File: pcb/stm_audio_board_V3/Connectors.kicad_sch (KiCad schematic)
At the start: 11 parts, among them J1 Power conn, J2 STlink, J3 Audio_sig, J4 Conn_01x01_taptempo, J4 Conn_01x10_display, J6 Conn_01x03_pot_ext, J7 Conn_01x8_pots_internal

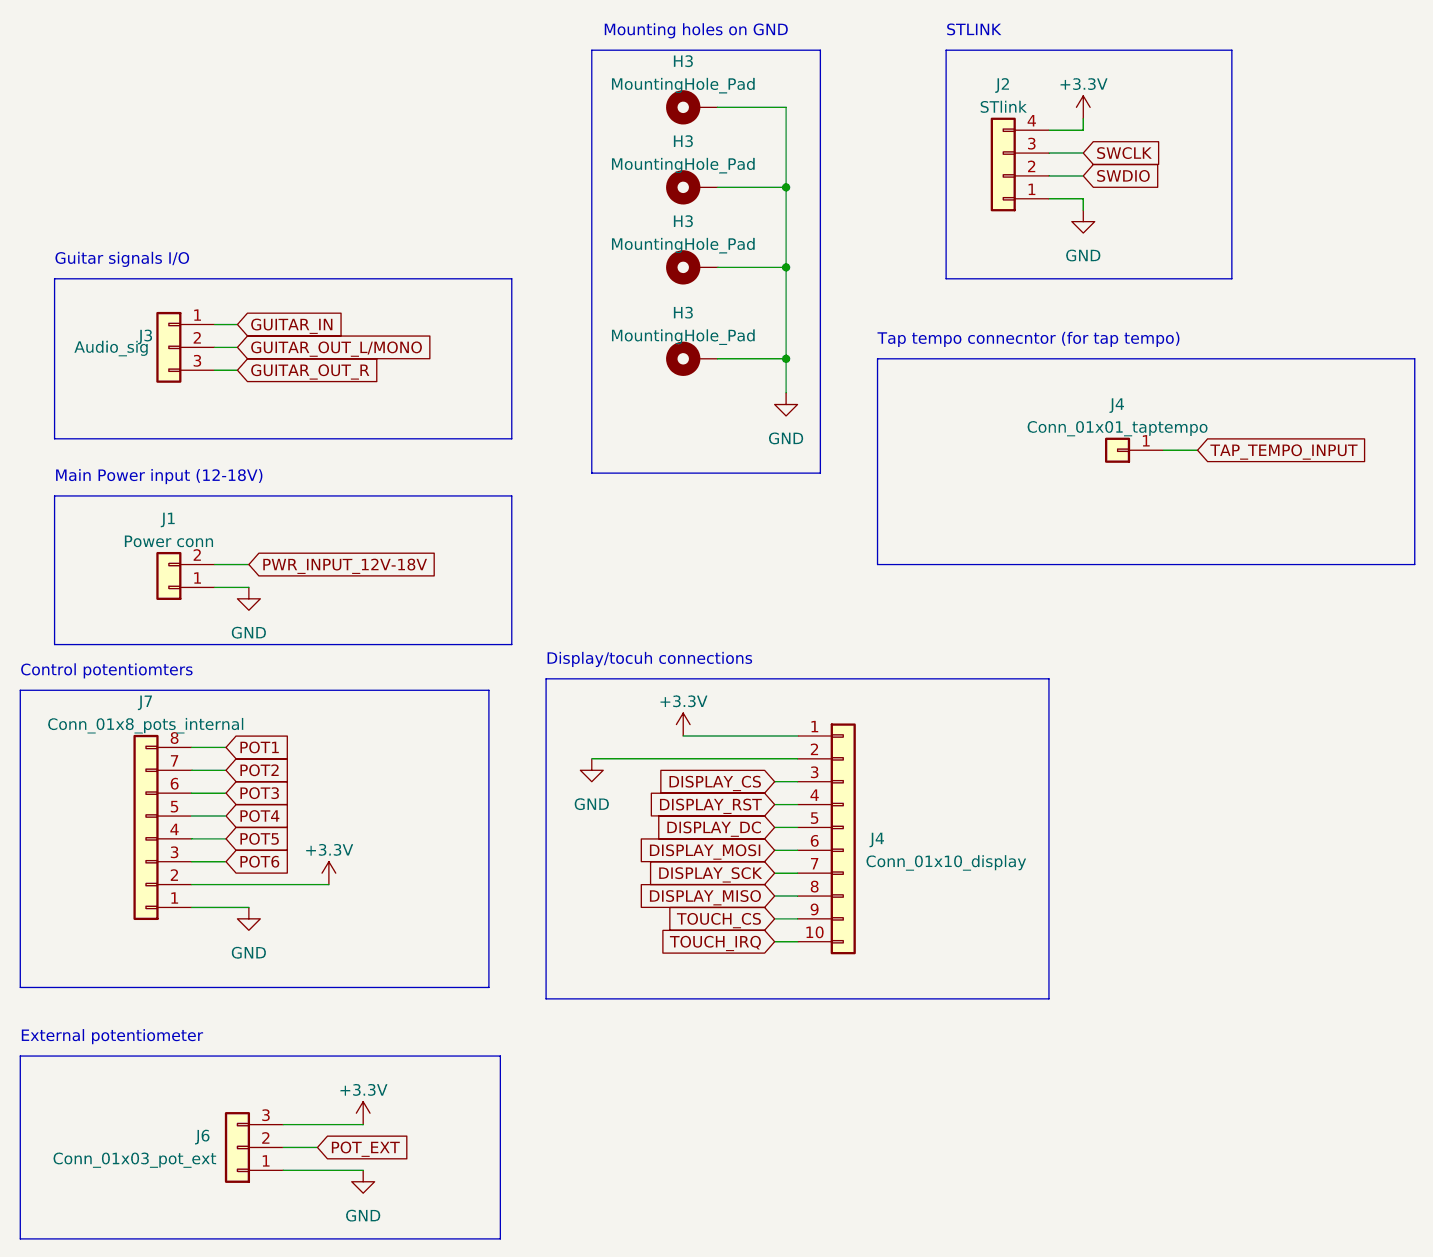
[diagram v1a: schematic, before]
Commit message: potmeter for V3 changed
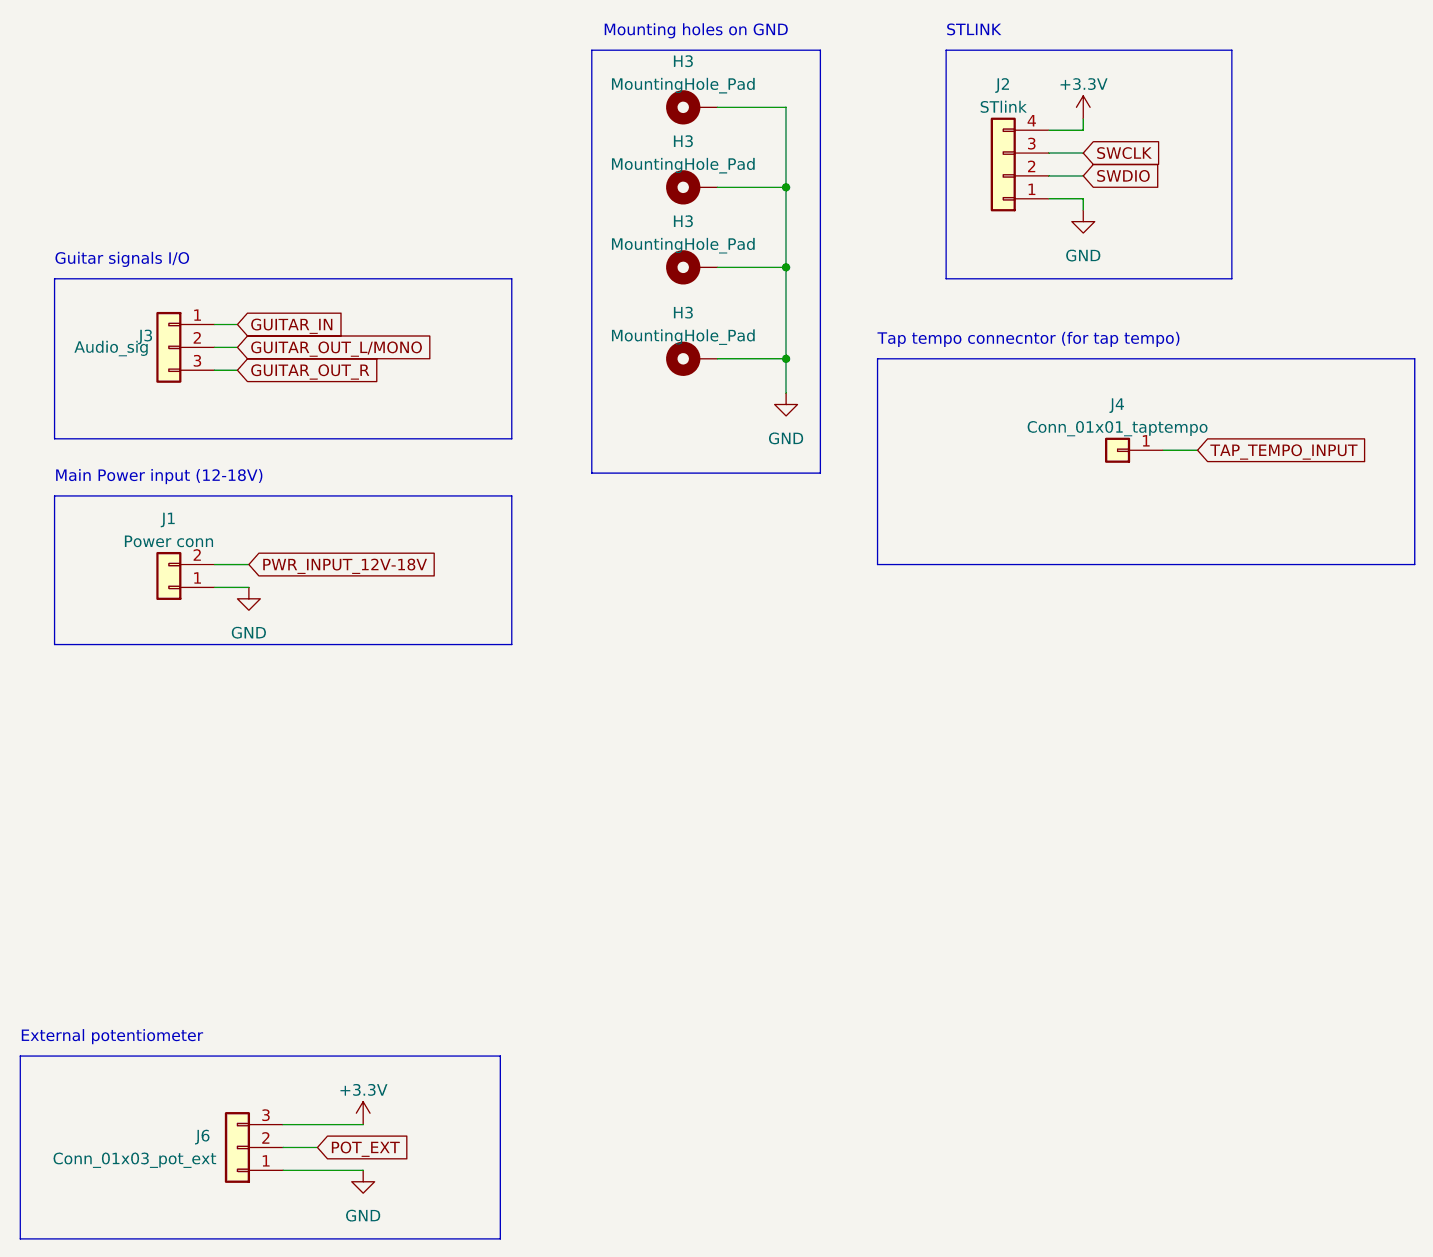
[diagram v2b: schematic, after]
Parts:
- removed J4: Conn_01x10_display, Connector_PinHeader_2.54mm:PinHeader_1x10_P2.54mm_Vertical, symbol Connector_Generic:Conn_01x10
- removed J7: Conn_01x8_pots_internal, Connector_PinHeader_2.54mm:PinHeader_1x08_P2.54mm_Vertical, symbol Connector_Generic:Conn_01x08
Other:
- note removed: "Control potentiomters"
- note removed: "Display/tocuh connections"
